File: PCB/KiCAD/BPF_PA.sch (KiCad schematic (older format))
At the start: 46 parts, among them J4 Conn_Coaxial, J5 Conn_Coaxial, J7 ANT, K1 TQ2-12VDC, Q11 BFG591, Q5 MMBT2222A, Q7 IRF610, T1 1_9, T3 1_4

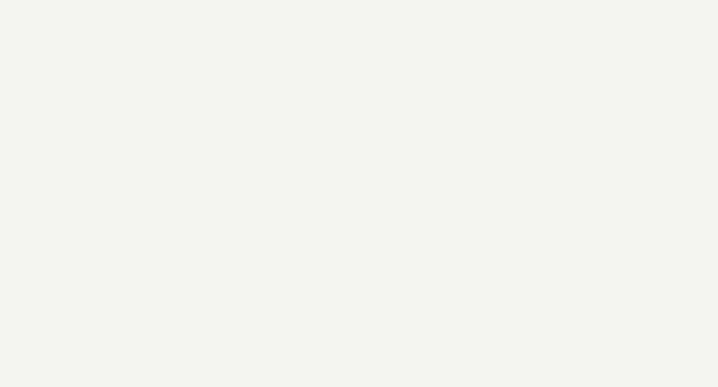
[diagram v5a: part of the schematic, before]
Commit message: PCB progress, IF TX, IF RX, PowerSupply Jack
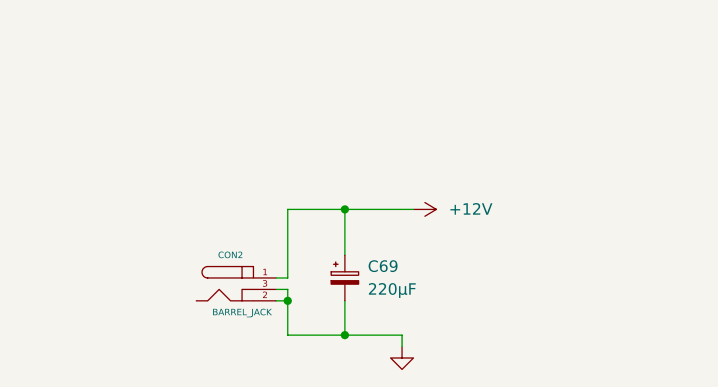
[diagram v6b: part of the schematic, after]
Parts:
- added C69: 220µF, DragonFly:CP_Radial_D6.3mm_P2.50mm, symbol CP_Small
- added CON2: BARREL_JACK, DragonFly:BARREL_JACK, symbol BARREL_JACK
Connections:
- net +12V: now also C69.1, CON2.1
- net GND: now also C69.2, CON2.2, CON2.3
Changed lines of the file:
@@
 $EndComp
 $Comp
-L GND #PWR93
+L GND #PWR95
 U 1 1 60FCFCEB
 P 3100 2900
-F 0 "#PWR93" H 3100 2650 50  0001 C CNN
+F 0 "#PWR95" H 3100 2650 50  0001 C CNN
 F 1 "GND" H 3100 2750 50  0001 C CNN
 F 2 "" H 3100 2900 50  0001 C CNN
@@
 $EndComp
 $Comp
-L GND #PWR98
+L GND #PWR100
 U 1 1 60FD0762
 P 5250 2800
-F 0 "#PWR98" H 5250 2550 50  0001 C CNN
+F 0 "#PWR100" H 5250 2550 50  0001 C CNN
 F 1 "GND" H 5250 2650 50  0001 C CNN
 F 2 "" H 5250 2800 50  0001 C CNN
@@
 $EndComp
 $Comp
-L GND #PWR102
+L GND #PWR104
 U 1 1 60FD078E
 P 6500 3100
-F 0 "#PWR102" H 6500 2850 50  0001 C CNN
+F 0 "#PWR104" H 6500 2850 50  0001 C CNN
 F 1 "GND" H 6500 2950 50  0001 C CNN
 F 2 "" H 6500 3100 50  0001 C CNN
@@
 $EndComp
 $Comp
-L GND #PWR105
+L GND #PWR107
 U 1 1 60FD07BA
 P 6700 3100
-F 0 "#PWR105" H 6700 2850 50  0001 C CNN
+F 0 "#PWR107" H 6700 2850 50  0001 C CNN
 F 1 "GND" H 6700 2950 50  0001 C CNN
 F 2 "" H 6700 3100 50  0001 C CNN
@@
 $EndComp
 $Comp
-L GND #PWR103
+L GND #PWR105
 U 1 1 60FD37CB
 P 6550 1450
-F 0 "#PWR103" H 6550 1200 50  0001 C CNN
+F 0 "#PWR105" H 6550 1200 50  0001 C CNN
 F 1 "GND" H 6550 1300 50  0001 C CNN
 F 2 "" H 6550 1450 50  0001 C CNN
@@
 $EndComp
 $Comp
-L GND #PWR101
+L GND #PWR103
 U 1 1 60FD3870
 P 5950 1450
-F 0 "#PWR101" H 5950 1200 50  0001 C CNN
+F 0 "#PWR103" H 5950 1200 50  0001 C CNN
 F 1 "GND" H 5950 1300 50  0001 C CNN
 F 2 "" H 5950 1450 50  0001 C CNN
@@
 $EndComp
 $Comp
-L GND #PWR116
+L GND #PWR118
 U 1 1 60FD3B07
 P 8700 2700
-F 0 "#PWR116" H 8700 2450 50  0001 C CNN
+F 0 "#PWR118" H 8700 2450 50  0001 C CNN
 F 1 "GND" H 8700 2550 50  0001 C CNN
 F 2 "" H 8700 2700 50  0001 C CNN
@@
 $EndComp
 $Comp
-L GND #PWR107
+L GND #PWR109
 U 1 1 60FD4018
 P 7400 3150
-F 0 "#PWR107" H 7400 2900 50  0001 C CNN
+F 0 "#PWR109" H 7400 2900 50  0001 C CNN
 F 1 "GND" H 7400 3000 50  0001 C CNN
 F 2 "" H 7400 3150 50  0001 C CNN
@@
 $EndComp
 $Comp
-L GND #PWR112
+L GND #PWR114
 U 1 1 60FD41CF
 P 8250 2850
-F 0 "#PWR112" H 8250 2600 50  0001 C CNN
+F 0 "#PWR114" H 8250 2600 50  0001 C CNN
 F 1 "GND" H 8250 2700 50  0001 C CNN
 F 2 "" H 8250 2850 50  0001 C CNN
@@
 $EndComp
 $Comp
-L GND #PWR114
+L GND #PWR116
 U 1 1 60FD63D0
 P 8300 1750
-F 0 "#PWR114" H 8300 1500 50  0001 C CNN
+F 0 "#PWR116" H 8300 1500 50  0001 C CNN
 F 1 "GND" H 8300 1600 50  0001 C CNN
 F 2 "" H 8300 1750 50  0001 C CNN
@@
 $EndComp
 $Comp
-L GND #PWR113
+L GND #PWR115
 U 1 1 60FD6513
 P 8300 1400
-F 0 "#PWR113" H 8300 1150 50  0001 C CNN
+F 0 "#PWR115" H 8300 1150 50  0001 C CNN
 F 1 "GND" H 8300 1250 50  0001 C CNN
 F 2 "" H 8300 1400 50  0001 C CNN
@@
 $EndComp
 $Comp
-L GND #PWR110
+L GND #PWR112
 U 1 1 60FD7124
 P 8200 3250
-F 0 "#PWR110" H 8200 3000 50  0001 C CNN
+F 0 "#PWR112" H 8200 3000 50  0001 C CNN
 F 1 "GND" H 8200 3100 50  0001 C CNN
 F 2 "" H 8200 3250 50  0001 C CNN
@@
 $EndComp
 $Comp
-L GND #PWR111
+L GND #PWR113
 U 1 1 60FD7200
 P 8200 3650
-F 0 "#PWR111" H 8200 3400 50  0001 C CNN
+F 0 "#PWR113" H 8200 3400 50  0001 C CNN
 F 1 "GND" H 8200 3500 50  0001 C CNN
 F 2 "" H 8200 3650 50  0001 C CNN
@@
 $EndComp
 $Comp
-L +12V #PWR97
+L +12V #PWR99
 U 1 1 60FD8C5E
 P 5000 1000
-F 0 "#PWR97" H 5000 850 50  0001 C CNN
+F 0 "#PWR99" H 5000 850 50  0001 C CNN
 F 1 "+12V" V 5000 1250 50  0000 C CNN
 F 2 "" H 5000 1000 50  0001 C CNN
@@
 $EndComp
 $Comp
-L +12V #PWR115
+L +12V #PWR117
 U 1 1 60FD8D87
 P 8700 850
-F 0 "#PWR115" H 8700 700 50  0001 C CNN
+F 0 "#PWR117" H 8700 700 50  0001 C CNN
 F 1 "+12V" H 8700 990 50  0000 C CNN
 F 2 "" H 8700 850 50  0001 C CNN
@@
 $EndComp
 $Comp
-L GND #PWR95
+L GND #PWR97
 U 1 1 60FDD9BB
 P 4600 3600
-F 0 "#PWR95" H 4600 3350 50  0001 C CNN
+F 0 "#PWR97" H 4600 3350 50  0001 C CNN
 F 1 "GND" H 4600 3450 50  0001 C CNN
 F 2 "" H 4600 3600 50  0001 C CNN
@@
 $EndComp
 $Comp
-L GND #PWR118
+L GND #PWR120
 U 1 1 60FE3B69
 P 9450 5450
-F 0 "#PWR118" H 9450 5200 50  0001 C CNN
+F 0 "#PWR120" H 9450 5200 50  0001 C CNN
 F 1 "GND" H 9450 5300 50  0001 C CNN
 F 2 "" H 9450 5450 50  0001 C CNN
@@
 $EndComp
 $Comp
-L GND #PWR109
+L GND #PWR111
 U 1 1 6105582E
 P 8050 5500
-F 0 "#PWR109" H 8050 5250 50  0001 C CNN
+F 0 "#PWR111" H 8050 5250 50  0001 C CNN
 F 1 "GND" H 8050 5350 50  0001 C CNN
 F 2 "" H 8050 5500 50  0001 C CNN
@@
 $EndComp
 $Comp
-L GND #PWR108
+L GND #PWR110
 U 1 1 61055A33
 P 7650 5500
-F 0 "#PWR108" H 7650 5250 50  0001 C CNN
+F 0 "#PWR110" H 7650 5250 50  0001 C CNN
 F 1 "GND" H 7650 5350 50  0001 C CNN
 F 2 "" H 7650 5500 50  0001 C CNN
@@
 $EndComp
 $Comp
-L GND #PWR117
+L GND #PWR119
 U 1 1 61055FE5
 P 8900 5750
-F 0 "#PWR117" H 8900 5500 50  0001 C CNN
+F 0 "#PWR119" H 8900 5500 50  0001 C CNN
 F 1 "GND" H 8900 5600 50  0001 C CNN
 F 2 "" H 8900 5750 50  0001 C CNN
@@
 $EndComp
 $Comp
-L GND #PWR100
+L GND #PWR102
 U 1 1 61056E24
 P 5850 5750
-F 0 "#PWR100" H 5850 5500 50  0001 C CNN
+F 0 "#PWR102" H 5850 5500 50  0001 C CNN
 F 1 "GND" H 5850 5600 50  0001 C CNN
 F 2 "" H 5850 5750 50  0001 C CNN
@@
 $EndComp
 $Comp
-L GND #PWR94
+L GND #PWR96
 U 1 1 612356A3
 P 4400 2900
-F 0 "#PWR94" H 4400 2650 50  0001 C CNN
+F 0 "#PWR96" H 4400 2650 50  0001 C CNN
 F 1 "GND" H 4400 2750 50  0001 C CNN
 F 2 "" H 4400 2900 50  0001 C CNN
@@
 Connection ~ 5300 5500
 $Comp
-L GND #PWR99
+L GND #PWR101
 U 1 1 61244496
 P 5300 5750
-F 0 "#PWR99" H 5300 5500 50  0001 C CNN
+F 0 "#PWR101" H 5300 5500 50  0001 C CNN
 F 1 "GND" H 5300 5600 50  0001 C CNN
 F 2 "" H 5300 5750 50  0001 C CNN
@@
 $EndComp
 $Comp
-L +12V #PWR96
+L +12V #PWR98
 U 1 1 61244868
 P 4600 4850
-F 0 "#PWR96" H 4600 4700 50  0001 C CNN
+F 0 "#PWR98" H 4600 4700 50  0001 C CNN
 F 1 "+12V" V 4600 5100 50  0000 C CNN
 F 2 "" H 4600 4850 50  0001 C CNN
@@
 Connection ~ 7200 5150
 $Comp
-L GND #PWR106
+L GND #PWR108
 U 1 1 6124C7E1
 P 7200 5500
-F 0 "#PWR106" H 7200 5250 50  0001 C CNN
+F 0 "#PWR108" H 7200 5250 50  0001 C CNN
 F 1 "GND" H 7200 5350 50  0001 C CNN
 F 2 "" H 7200 5500 50  0001 C CNN
@@
 	7200 5500 7200 5450
 $Comp
-L GND #PWR104
+L GND #PWR106
 U 1 1 6124C940
 P 6650 5500
-F 0 "#PWR104" H 6650 5250 50  0001 C CNN
+F 0 "#PWR106" H 6650 5250 50  0001 C CNN
 F 1 "GND" H 6650 5350 50  0001 C CNN
 F 2 "" H 6650 5500 50  0001 C CNN
@@
 	0    -1   -1   0
 $EndComp
+$Comp
+L BARREL_JACK CON2
+U 1 1 6126FC70
+P 1800 5550
+F 0 "CON2" H 1900 5650 28  0000 C CNN
+F 1 "BARREL_JACK" H 1950 5400 28  0000 C CNN
+F 2 "DragonFly:BARREL_JACK" H 1800 5550 50  0001 C CNN
+F 3 "" H 1800 5550 50  0000 C CNN
+	1    1800 5550
+	1    0    0    -1
+$EndComp
+$Comp
+L +12V #PWR94
+U 1 1 6126FE6E
+P 2700 5250
+F 0 "#PWR94" H 2700 5100 50  0001 C CNN
+F 1 "+12V" V 2700 5500 50  0000 C CNN
+F 2 "" H 2700 5250 50  0001 C CNN
+F 3 "" H 2700 5250 50  0001 C CNN
+	1    2700 5250
+	0    1    1    0
+$EndComp
+$Comp
+L GND #PWR93
+U 1 1 612713A0
+P 2650 5850
+F 0 "#PWR93" H 2650 5600 50  0001 C CNN
+F 1 "GND" H 2650 5700 50  0001 C CNN
+F 2 "" H 2650 5850 50  0001 C CNN
+F 3 "" H 2650 5850 50  0001 C CNN
+	1    2650 5850
+	1    0    0    -1
+$EndComp
+Wire Wire Line
+	2100 5600 2150 5600
+Wire Wire Line
+	2150 5600 2150 5800
+Wire Wire Line
+	2150 5650 2100 5650
+Wire Wire Line
+	2150 5800 2650 5800
+Wire Wire Line
+	2650 5800 2650 5850
+Connection ~ 2150 5650
+Wire Wire Line
+	2700 5250 2150 5250
+Wire Wire Line
+	2150 5250 2150 5550
+Wire Wire Line
+	2150 5550 2100 5550
+$Comp
+L CP_Small C69
+U 1 1 61271AE6
+P 2400 5550
+F 0 "C69" H 2500 5600 50  0000 L CNN
+F 1 "220µF" H 2500 5500 50  0000 L CNN
+F 2 "DragonFly:CP_Radial_D6.3mm_P2.50mm" H 2400 5550 50  0001 C CNN
+F 3 "" H 2400 5550 50  0001 C CNN
+	1    2400 5550
+	1    0    0    -1
+$EndComp
+Wire Wire Line
+	2400 5450 2400 5250
+Connection ~ 2400 5250
+Wire Wire Line
+	2400 5650 2400 5800
+Connection ~ 2400 5800
 $EndSCHEMATC

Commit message: PCB progress, fix MMBFJ310 error
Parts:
- Q7: footprint DragonFly:TO-220_Neutral123_Horizontal_LargePads -> DragonFly:TO-220_Neutral123_Horizontal_LargePads_BigHole
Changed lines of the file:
@@
 $EndComp
 $Comp
-L GND #PWR094
+L GND #PWR98
 U 1 1 60FCFCEB
 P 3100 2900
-F 0 "#PWR094" H 3100 2650 50  0001 C CNN
+F 0 "#PWR98" H 3100 2650 50  0001 C CNN
 F 1 "GND" H 3100 2750 50  0001 C CNN
 F 2 "" H 3100 2900 50  0001 C CNN
@@
 $EndComp
 $Comp
-L GND #PWR095
+L GND #PWR103
 U 1 1 60FD0762
 P 5250 2800
-F 0 "#PWR095" H 5250 2550 50  0001 C CNN
+F 0 "#PWR103" H 5250 2550 50  0001 C CNN
 F 1 "GND" H 5250 2650 50  0001 C CNN
 F 2 "" H 5250 2800 50  0001 C CNN
@@
 $EndComp
 $Comp
-L GND #PWR096
+L GND #PWR107
 U 1 1 60FD078E
 P 6500 3100
-F 0 "#PWR096" H 6500 2850 50  0001 C CNN
+F 0 "#PWR107" H 6500 2850 50  0001 C CNN
 F 1 "GND" H 6500 2950 50  0001 C CNN
 F 2 "" H 6500 3100 50  0001 C CNN
@@
 $EndComp
 $Comp
-L GND #PWR097
+L GND #PWR110
 U 1 1 60FD07BA
 P 6700 3100
-F 0 "#PWR097" H 6700 2850 50  0001 C CNN
+F 0 "#PWR110" H 6700 2850 50  0001 C CNN
 F 1 "GND" H 6700 2950 50  0001 C CNN
 F 2 "" H 6700 3100 50  0001 C CNN
@@
 $EndComp
 $Comp
-L GND #PWR098
+L GND #PWR108
 U 1 1 60FD37CB
 P 6550 1450
-F 0 "#PWR098" H 6550 1200 50  0001 C CNN
+F 0 "#PWR108" H 6550 1200 50  0001 C CNN
 F 1 "GND" H 6550 1300 50  0001 C CNN
 F 2 "" H 6550 1450 50  0001 C CNN
@@
 $EndComp
 $Comp
-L GND #PWR099
+L GND #PWR106
 U 1 1 60FD3870
 P 5950 1450
-F 0 "#PWR099" H 5950 1200 50  0001 C CNN
+F 0 "#PWR106" H 5950 1200 50  0001 C CNN
 F 1 "GND" H 5950 1300 50  0001 C CNN
 F 2 "" H 5950 1450 50  0001 C CNN
@@
 $EndComp
 $Comp
-L GND #PWR0100
+L GND #PWR121
 U 1 1 60FD3B07
 P 8700 2700
-F 0 "#PWR0100" H 8700 2450 50  0001 C CNN
+F 0 "#PWR121" H 8700 2450 50  0001 C CNN
 F 1 "GND" H 8700 2550 50  0001 C CNN
 F 2 "" H 8700 2700 50  0001 C CNN
@@
 $EndComp
 $Comp
-L GND #PWR0101
+L GND #PWR112
 U 1 1 60FD4018
 P 7400 3150
-F 0 "#PWR0101" H 7400 2900 50  0001 C CNN
+F 0 "#PWR112" H 7400 2900 50  0001 C CNN
 F 1 "GND" H 7400 3000 50  0001 C CNN
 F 2 "" H 7400 3150 50  0001 C CNN
@@
 $EndComp
 $Comp
-L GND #PWR0102
+L GND #PWR117
 U 1 1 60FD41CF
 P 8250 2850
-F 0 "#PWR0102" H 8250 2600 50  0001 C CNN
+F 0 "#PWR117" H 8250 2600 50  0001 C CNN
 F 1 "GND" H 8250 2700 50  0001 C CNN
 F 2 "" H 8250 2850 50  0001 C CNN
@@
 $EndComp
 $Comp
-L GND #PWR0103
+L GND #PWR119
 U 1 1 60FD63D0
 P 8300 1750
-F 0 "#PWR0103" H 8300 1500 50  0001 C CNN
+F 0 "#PWR119" H 8300 1500 50  0001 C CNN
 F 1 "GND" H 8300 1600 50  0001 C CNN
 F 2 "" H 8300 1750 50  0001 C CNN
@@
 $EndComp
 $Comp
-L GND #PWR0104
+L GND #PWR118
 U 1 1 60FD6513
 P 8300 1400
-F 0 "#PWR0104" H 8300 1150 50  0001 C CNN
+F 0 "#PWR118" H 8300 1150 50  0001 C CNN
 F 1 "GND" H 8300 1250 50  0001 C CNN
 F 2 "" H 8300 1400 50  0001 C CNN
@@
 $EndComp
 $Comp
-L GND #PWR0105
+L GND #PWR115
 U 1 1 60FD7124
 P 8200 3250
-F 0 "#PWR0105" H 8200 3000 50  0001 C CNN
+F 0 "#PWR115" H 8200 3000 50  0001 C CNN
 F 1 "GND" H 8200 3100 50  0001 C CNN
 F 2 "" H 8200 3250 50  0001 C CNN
@@
 $EndComp
 $Comp
-L GND #PWR0106
+L GND #PWR116
 U 1 1 60FD7200
 P 8200 3650
-F 0 "#PWR0106" H 8200 3400 50  0001 C CNN
+F 0 "#PWR116" H 8200 3400 50  0001 C CNN
 F 1 "GND" H 8200 3500 50  0001 C CNN
 F 2 "" H 8200 3650 50  0001 C CNN
@@
 $EndComp
 $Comp
-L +12V #PWR0107
+L +12V #PWR102
 U 1 1 60FD8C5E
 P 5000 1000
-F 0 "#PWR0107" H 5000 850 50  0001 C CNN
+F 0 "#PWR102" H 5000 850 50  0001 C CNN
 F 1 "+12V" V 5000 1250 50  0000 C CNN
 F 2 "" H 5000 1000 50  0001 C CNN
@@
 $EndComp
 $Comp
-L +12V #PWR0108
+L +12V #PWR120
 U 1 1 60FD8D87
 P 8700 850
-F 0 "#PWR0108" H 8700 700 50  0001 C CNN
+F 0 "#PWR120" H 8700 700 50  0001 C CNN
 F 1 "+12V" H 8700 990 50  0000 C CNN
 F 2 "" H 8700 850 50  0001 C CNN
@@
 $EndComp
 $Comp
-L GND #PWR0109
+L GND #PWR95
 U 1 1 60FDD885
 P 1750 3600
-F 0 "#PWR0109" H 1750 3350 50  0001 C CNN
+F 0 "#PWR95" H 1750 3350 50  0001 C CNN
 F 1 "GND" H 1750 3450 50  0001 C CNN
 F 2 "" H 1750 3600 50  0001 C CNN
@@
 $EndComp
 $Comp
-L GND #PWR0110
+L GND #PWR100
 U 1 1 60FDD9BB
 P 4600 3600
-F 0 "#PWR0110" H 4600 3350 50  0001 C CNN
+F 0 "#PWR100" H 4600 3350 50  0001 C CNN
 F 1 "GND" H 4600 3450 50  0001 C CNN
 F 2 "" H 4600 3600 50  0001 C CNN
@@
 $EndComp
 $Comp
-L GND #PWR0111
+L GND #PWR123
 U 1 1 60FE3B69
 P 9450 5450
-F 0 "#PWR0111" H 9450 5200 50  0001 C CNN
+F 0 "#PWR123" H 9450 5200 50  0001 C CNN
 F 1 "GND" H 9450 5300 50  0001 C CNN
 F 2 "" H 9450 5450 50  0001 C CNN
@@
 $EndComp
 $Comp
-L GND #PWR0112
+L GND #PWR114
 U 1 1 6105582E
 P 8050 5500
-F 0 "#PWR0112" H 8050 5250 50  0001 C CNN
+F 0 "#PWR114" H 8050 5250 50  0001 C CNN
 F 1 "GND" H 8050 5350 50  0001 C CNN
 F 2 "" H 8050 5500 50  0001 C CNN
@@
 $EndComp
 $Comp
-L GND #PWR0113
+L GND #PWR113
 U 1 1 61055A33
 P 7650 5500
-F 0 "#PWR0113" H 7650 5250 50  0001 C CNN
+F 0 "#PWR113" H 7650 5250 50  0001 C CNN
 F 1 "GND" H 7650 5350 50  0001 C CNN
 F 2 "" H 7650 5500 50  0001 C CNN
@@
 $EndComp
 $Comp
-L GND #PWR0114
+L GND #PWR122
 U 1 1 61055FE5
 P 8900 5750
-F 0 "#PWR0114" H 8900 5500 50  0001 C CNN
+F 0 "#PWR122" H 8900 5500 50  0001 C CNN
 F 1 "GND" H 8900 5600 50  0001 C CNN
 F 2 "" H 8900 5750 50  0001 C CNN
@@
 $EndComp
 $Comp
-L GND #PWR0115
+L GND #PWR105
 U 1 1 61056E24
 P 5850 5750
-F 0 "#PWR0115" H 5850 5500 50  0001 C CNN
+F 0 "#PWR105" H 5850 5500 50  0001 C CNN
 F 1 "GND" H 5850 5600 50  0001 C CNN
 F 2 "" H 5850 5750 50  0001 C CNN
@@
 $EndComp
 $Comp
-L GND #PWR0116
+L GND #PWR94
 U 1 1 612355AA
 P 1750 2900
-F 0 "#PWR0116" H 1750 2650 50  0001 C CNN
+F 0 "#PWR94" H 1750 2650 50  0001 C CNN
 F 1 "GND" H 1750 2750 50  0001 C CNN
 F 2 "" H 1750 2900 50  0001 C CNN
@@
 $EndComp
 $Comp
-L GND #PWR0117
+L GND #PWR99
 U 1 1 612356A3
 P 4400 2900
-F 0 "#PWR0117" H 4400 2650 50  0001 C CNN
+F 0 "#PWR99" H 4400 2650 50  0001 C CNN
 F 1 "GND" H 4400 2750 50  0001 C CNN
 F 2 "" H 4400 2900 50  0001 C CNN
@@
 Connection ~ 5300 5500
 $Comp
-L GND #PWR0118
+L GND #PWR104
 U 1 1 61244496
 P 5300 5750
-F 0 "#PWR0118" H 5300 5500 50  0001 C CNN
+F 0 "#PWR104" H 5300 5500 50  0001 C CNN
 F 1 "GND" H 5300 5600 50  0001 C CNN
 F 2 "" H 5300 5750 50  0001 C CNN
@@
 $EndComp
 $Comp
-L +12V #PWR0119
+L +12V #PWR101
 U 1 1 61244868
 P 4600 4850
-F 0 "#PWR0119" H 4600 4700 50  0001 C CNN
+F 0 "#PWR101" H 4600 4700 50  0001 C CNN
 F 1 "+12V" V 4600 5100 50  0000 C CNN
 F 2 "" H 4600 4850 50  0001 C CNN
@@
 Connection ~ 7200 5150
 $Comp
-L GND #PWR0120
+L GND #PWR111
 U 1 1 6124C7E1
 P 7200 5500
-F 0 "#PWR0120" H 7200 5250 50  0001 C CNN
+F 0 "#PWR111" H 7200 5250 50  0001 C CNN
 F 1 "GND" H 7200 5350 50  0001 C CNN
 F 2 "" H 7200 5500 50  0001 C CNN
@@
 	7200 5500 7200 5450
 $Comp
-L GND #PWR0121
+L GND #PWR109
 U 1 1 6124C940
 P 6650 5500
-F 0 "#PWR0121" H 6650 5250 50  0001 C CNN
+F 0 "#PWR109" H 6650 5250 50  0001 C CNN
 F 1 "GND" H 6650 5350 50  0001 C CNN
 F 2 "" H 6650 5500 50  0001 C CNN
@@
 F 0 "Q7" H 8800 2500 50  0000 L CNN
 F 1 "IRF610" H 8800 2400 50  0000 L CNN
-F 2 "DragonFly:TO-220_Neutral123_Horizontal_LargePads" H 8800 2550 50  0001 C CNN
+F 2 "DragonFly:TO-220_Neutral123_Horizontal_LargePads_BigHole" H 8800 2550 50  0001 C CNN
 F 3 "" H 8600 2450 50  0001 C CNN
 	1    8600 2450
@@
 $EndComp
 $Comp
-L +12V #PWR0122
+L +12V #PWR97
 U 1 1 6126FE6E
 P 2700 5250
-F 0 "#PWR0122" H 2700 5100 50  0001 C CNN
+F 0 "#PWR97" H 2700 5100 50  0001 C CNN
 F 1 "+12V" V 2700 5500 50  0000 C CNN
 F 2 "" H 2700 5250 50  0001 C CNN
@@
 $EndComp
 $Comp
-L GND #PWR0123
+L GND #PWR96
 U 1 1 612713A0
 P 2650 5850
-F 0 "#PWR0123" H 2650 5600 50  0001 C CNN
+F 0 "#PWR96" H 2650 5600 50  0001 C CNN
 F 1 "GND" H 2650 5700 50  0001 C CNN
 F 2 "" H 2650 5850 50  0001 C CNN
